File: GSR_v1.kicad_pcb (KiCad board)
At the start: 2 copper layers, 32.2 x 20.5 mm, 62 parts, among them P1 CONN_2, P2 CONN_2, P3 CONN_2, P4 CONN_2, Q1 DMP21D5UFB4-7B, U1 TPS63001, U2 LM324N, U3 NRF528XX-QFAA, U4 TMP116, U5 TPS2294x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

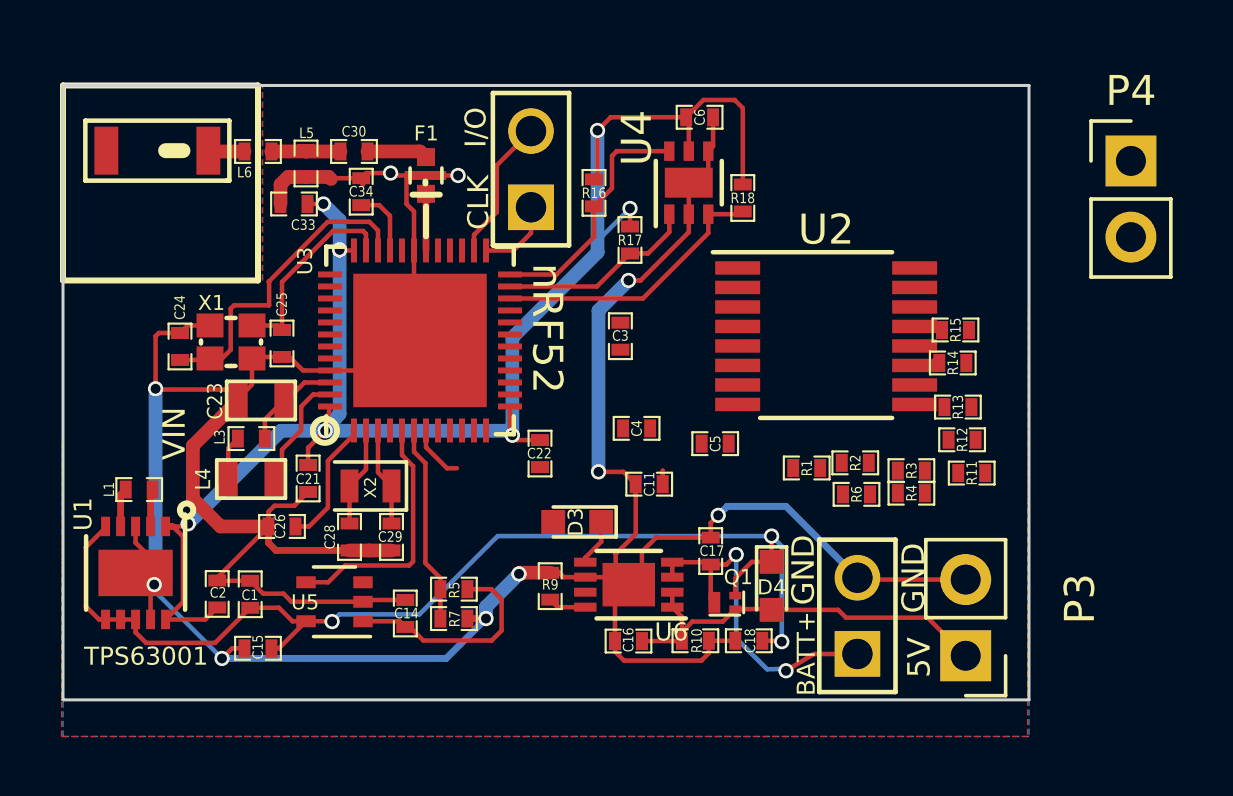
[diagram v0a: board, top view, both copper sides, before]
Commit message: Upgraded to KiCAD 5.0 compat
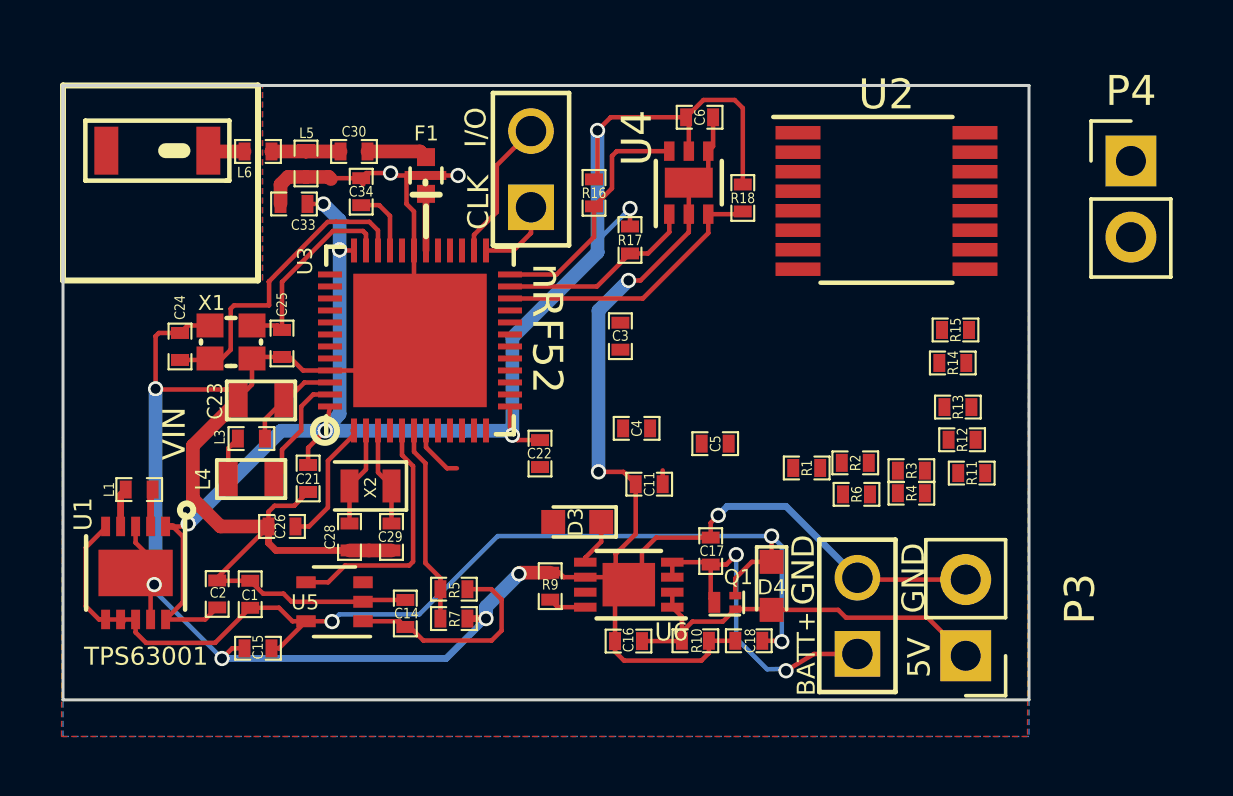
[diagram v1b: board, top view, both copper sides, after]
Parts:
- moved U2 4.94 mm to (293.4, 129.3)
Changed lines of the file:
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@@
 (kicad_pcb (version 4) (host pcbnew 4.0.6)
   (general
-    (links 162)
+    (links 0)
     (no_connects 33)
-    (area 265.849999 125.449999 298.150001 146.030001)
+    (area 264.8176 122.157123 320.907143 147.200001)
     (thickness 1.6)
     (drawings 26)
@@
   )
   (module Housings_SSOP:TSSOP-16_4.4x5mm_Pitch0.65mm (layer F.Cu)
-    (at 291.338 133.858)
+    (at 293.35 129.35)
     (descr "16-Lead Plastic Thin Shrink Small Outline (ST)-4.4 mm Body [TSSOP] (see Microchip Packaging Specification 00000049BS.pdf)")
     (tags "SSOP 0.65")

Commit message: Updated footprint for LM324
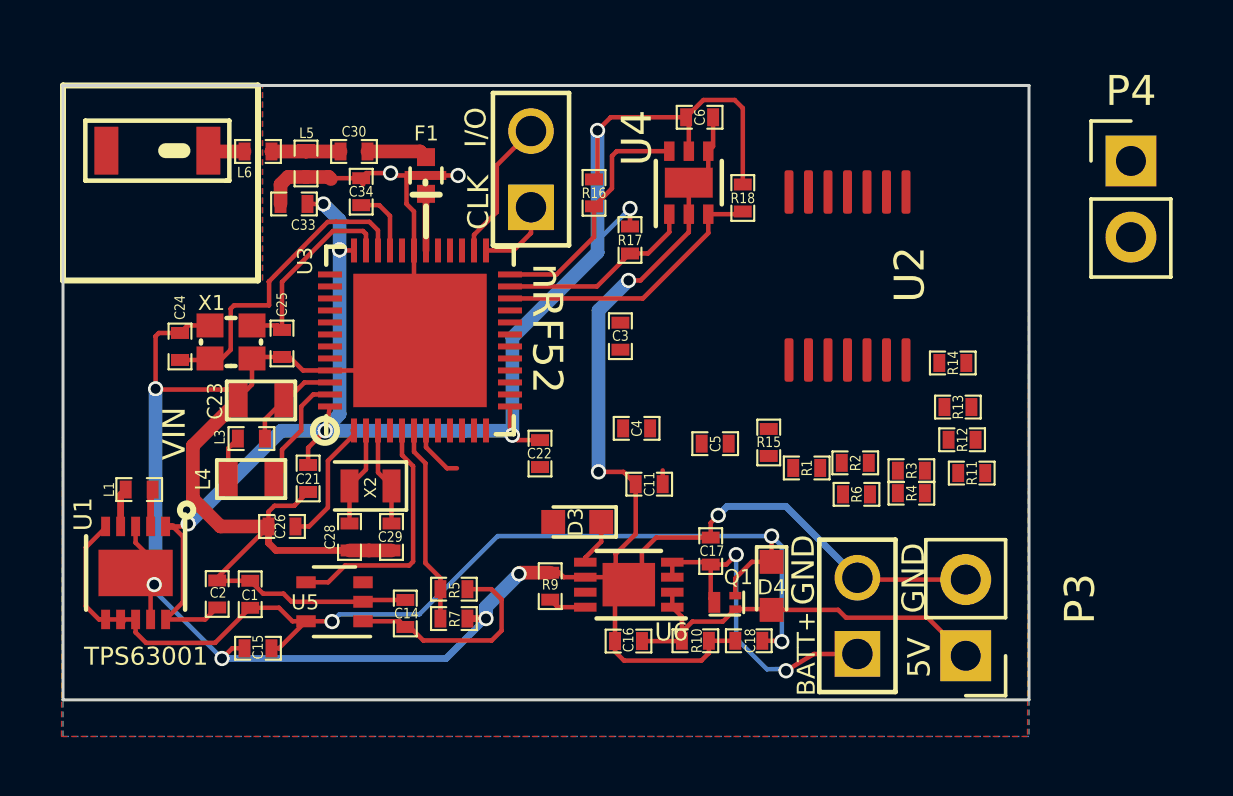
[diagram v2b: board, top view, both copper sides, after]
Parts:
- U2: footprint Housings_SSOP:TSSOP-16_4.4x5mm_Pitch0.65mm -> musaPwrPad:TSSOP-14_6.4x5mm
- moved R15 7.27 mm to (289.4, 137.4), turned to 270 degrees
- moved U2 2.82 mm to (292.1, 131.8), turned to 270 degrees

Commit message: Nathan edits and my finalization to PCB design.
Co-Authored-By: nzavanelli <nzavanelli@users.noreply.github.com>
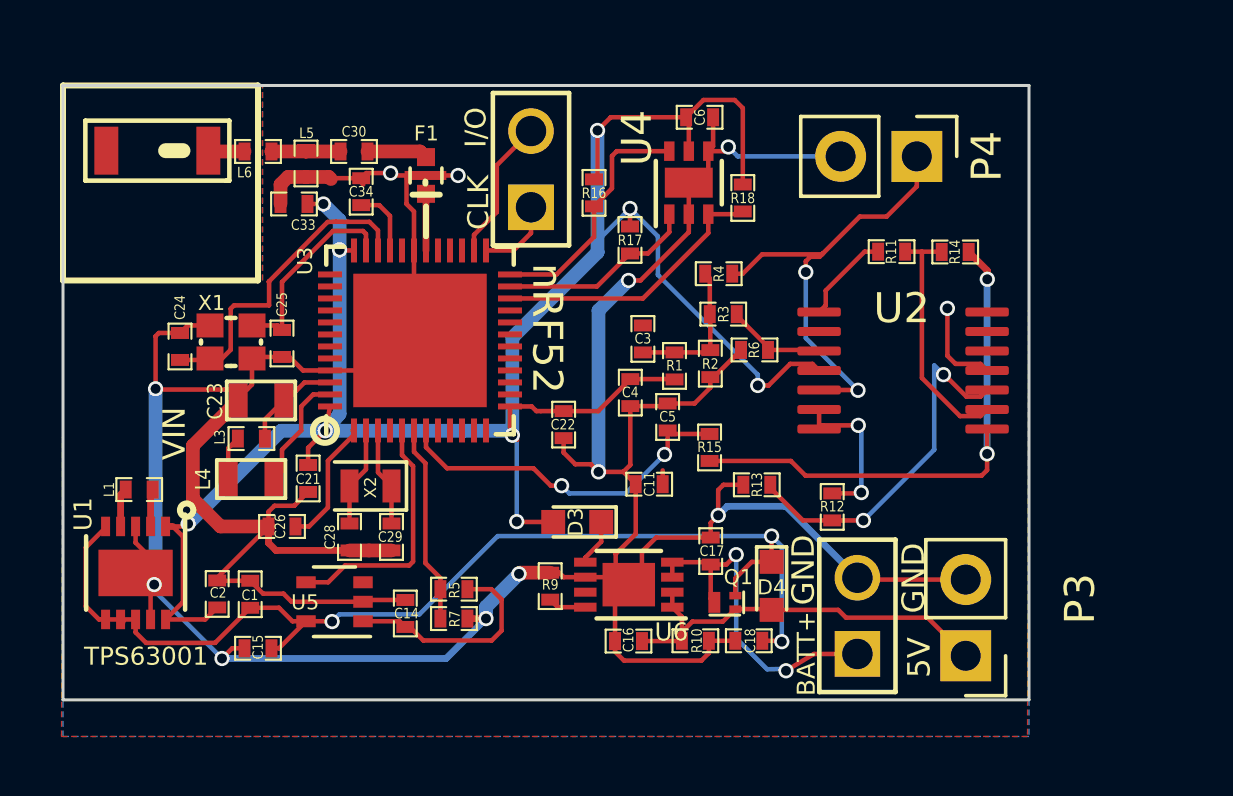
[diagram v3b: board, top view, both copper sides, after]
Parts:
- moved R4 9.73 mm to (287.8, 131.8)
- moved R3 8.16 mm to (287.9, 133.1)
- moved R11 7.85 mm to (293.5, 131.0), turned to 0 degrees
- moved R13 7.19 mm to (289.0, 138.8)
- moved P4 7.14 mm to (294.4, 127.9), turned to 270 degrees
- moved R6 5.89 mm to (289.0, 134.3), turned to 0 degrees
- moved R2 5.86 mm to (287.5, 134.8), turned to 90 degrees
- moved R1 5.57 mm to (286.3, 134.8), turned to 270 degrees
- moved R12 4.87 mm to (291.5, 139.5), turned to 270 degrees
- moved R14 3.70 mm to (295.6, 131.1), turned to 0 degrees
- moved U2 3.66 mm to (293.9, 135.0), turned to 0 degrees
- moved R15 1.98 mm to (287.5, 137.6)
- moved C5 1.82 mm to (286.1, 136.6), turned to 270 degrees
- moved C22 1.25 mm to (282.6, 136.8)
- moved C4 1.21 mm to (284.8, 135.7), turned to 270 degrees
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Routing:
- net DVDD: track 56.5 -> 76.1 mm, vias 7 -> 9
- net DGND: track 136.9 -> 155.2 mm, vias 10 -> 12
- net Net-(R14-Pad2): track 0.00 -> 17.9 mm, vias 0 -> 2
- net /ELECTRODE_INPUT: track 0.00 -> 15.4 mm, vias 0 -> 2
- net Net-(R12-Pad2): track 0.00 -> 12.1 mm, vias 0 -> 2
- net /GSR_AIN: track 1.88 -> 12.0 mm, vias 0 -> 2
- net Net-(R11-Pad2): track 0.00 -> 8.23 mm
- net Net-(R12-Pad1): track 0.00 -> 5.27 mm, vias 0 -> 2
- net Net-(C3-Pad2): track 0.00 -> 4.90 mm
- net Net-(R3-Pad1): track 0.00 -> 3.34 mm
- net Net-(R11-Pad1): track 0.00 -> 3.09 mm

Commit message: Fixed missing connections, resolved issues.
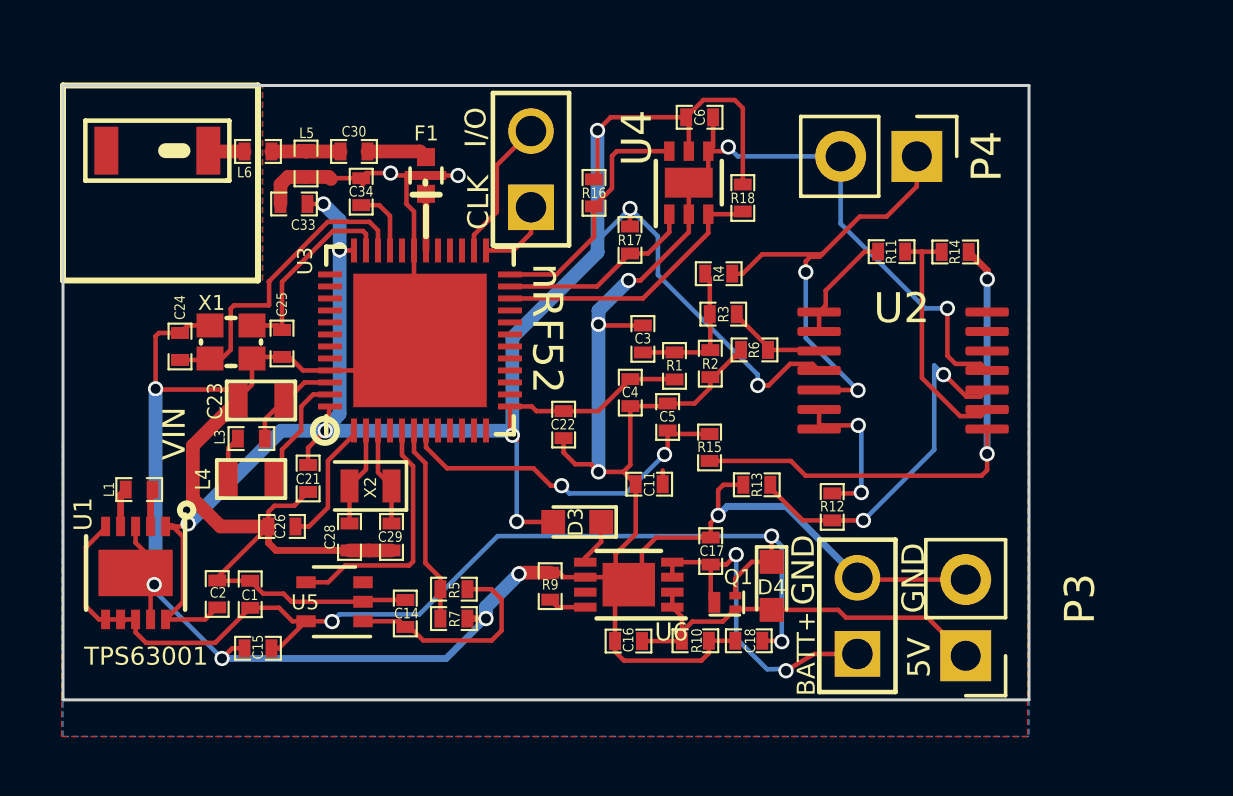
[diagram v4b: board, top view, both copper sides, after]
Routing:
- net DGND: track 155.2 -> 163.7 mm, vias 12 -> 13
- net Net-(R11-Pad1): track 3.09 -> 3.74 mm
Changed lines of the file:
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@@
     (thickness 1.6)
     (drawings 26)
-    (tracks 532)
+    (tracks 540)
     (zones 0)
     (modules 62)
@@
   (segment (start 286.76 129.79) (end 286.76 130.39) (width 0.152) (layer F.Cu) (net 37))
   (via (at 283.75 138.38) (size 0.508) (drill 0.3302) (layers F.Cu B.Cu) (net 37))
-  (segment (start 283.75 133) (end 283.75 138.38) (width 0.4572) (layer B.Cu) (net 37))
   (segment (start 284.75 132) (end 283.75 133) (width 0.4572) (layer B.Cu) (net 37))
   (via (at 284.75 132) (size 0.508) (drill 0.3302) (layers F.Cu B.Cu) (net 37))
@@
   (segment (start 295.65029 134.78029) (end 295.38 134.51) (width 0.152) (layer F.Cu) (net 37))
   (segment (start 295.38 134.51) (end 295.38 132.93) (width 0.152) (layer F.Cu) (net 37))
+  (via (at 283.75 133.46) (size 0.508) (drill 0.3302) (layers F.Cu B.Cu) (net 37))
+  (segment (start 283.75 133.46) (end 283.75 138.38) (width 0.4572) (layer B.Cu) (net 37))
+  (segment (start 283.75 133) (end 283.75 133.46) (width 0.4572) (layer B.Cu) (net 37))
+  (segment (start 283.78916 133.49916) (end 283.75 133.46) (width 0.152) (layer F.Cu) (net 37))
+  (segment (start 285.23 133.49916) (end 283.78916 133.49916) (width 0.152) (layer F.Cu) (net 37))
+  (segment (start 295.38 132.93) (end 294.65 132.93) (width 0.152) (layer B.Cu) (net 37))
+  (segment (start 291.8206 130.1006) (end 291.8206 127.8636) (width 0.152) (layer B.Cu) (net 37))
+  (segment (start 294.65 132.93) (end 291.8206 130.1006) (width 0.152) (layer B.Cu) (net 37))
   (segment (start 287.4772 133.13918) (end 287.45942 133.1214) (width 0.152) (layer F.Cu) (net 38))
   (segment (start 287.4772 134.32282) (end 287.4772 133.13918) (width 0.152) (layer F.Cu) (net 38))
@@
   (segment (start 292.62 131.04) (end 293.07084 131.04) (width 0.152) (layer F.Cu) (net 55))
   (segment (start 291.32411 132.33589) (end 292.62 131.04) (width 0.152) (layer F.Cu) (net 55))
+  (segment (start 291.1034 133.701) (end 291.1034 133.051) (width 0.152) (layer F.Cu) (net 55))
   (segment (start 295.18042 131.04) (end 295.19042 131.05) (width 0.152) (layer F.Cu) (net 56))
   (segment (start 296.48269 136.52171) (end 295.80171 136.52171) (width 0.152) (layer F.Cu) (net 56))

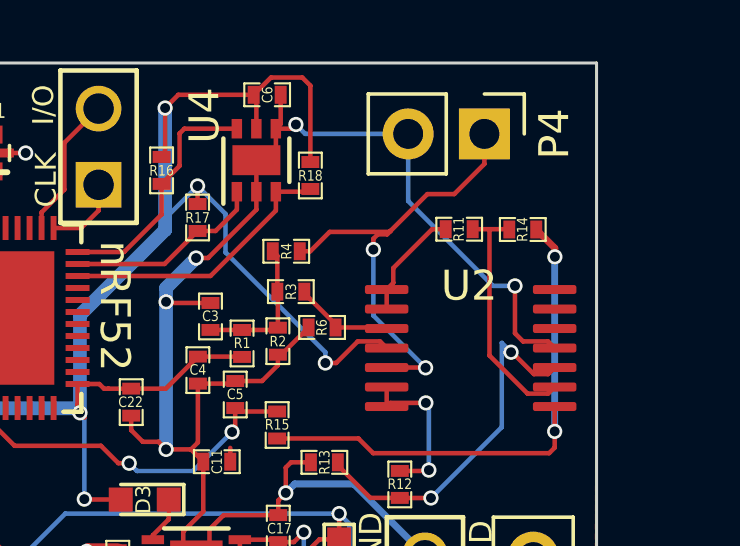
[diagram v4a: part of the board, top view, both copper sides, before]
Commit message: Updated Gerbers, deleted old gerber files, minor details. Updated silkscreen (back)
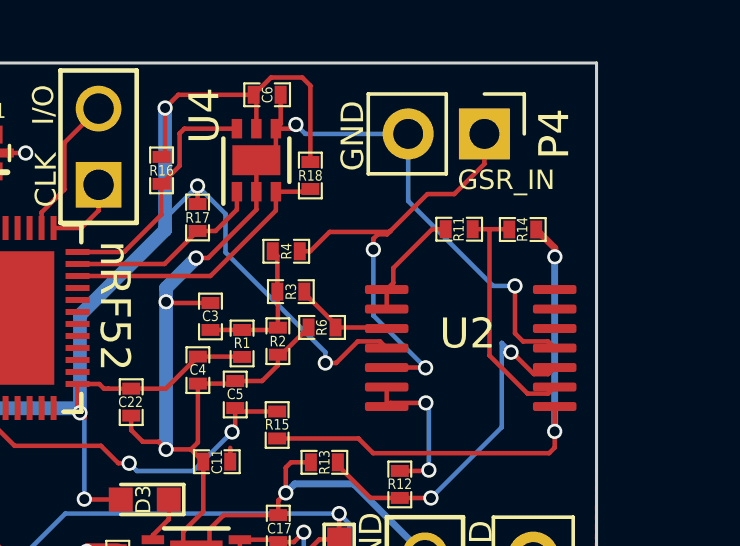
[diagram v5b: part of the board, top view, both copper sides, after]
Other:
- board text added: "GSR_IN"
- board text added: "nRF52-GSR Prototype 09/03/18 Yeo GaTech BNE Lab"
- board text removed: "nRF52-ADS1292-MPU ExG Prototype - 06/08/18 Yeo GaTech BNE Lab"
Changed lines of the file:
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@@
   (general
     (thickness 1.6)
-    (drawings 26)
+    (drawings 28)
     (tracks 540)
     (zones 0)
@@
     (34 B.Paste user)
     (35 F.Paste user hide)
-    (36 B.SilkS user hide)
+    (36 B.SilkS user)
     (37 F.SilkS user)
     (38 B.Mask user hide)
@@
   )
   (setup
-    (last_trace_width 0.152)
+    (last_trace_width 0.4572)
     (user_trace_width 0.152)
     (user_trace_width 0.229)
@@
     (visible_elements 7FFEFFBF)
     (pcbplotparams
-      (layerselection 0x010f0_80000001)
+      (layerselection 0x010f0_ffffffff)
       (usegerberextensions true)
       (usegerberattributes false)
@@
   (module musaPwrPad:TSSOP-14_6.4x5mm (layer F.Cu)
     (at 293.9034 135.001)
-    (fp_text reference U2 (at -0.05 -2.075 180) (layer F.SilkS)
+    (fp_text reference U2 (at -0.1034 -0.481 180) (layer F.SilkS)
       (effects (font (size 1 1) (thickness 0.15)))
     )
@@
       (net 9 DVDD))
   )
+  (gr_text GSR_IN (at 295.09 129.4) (layer F.SilkS)
+    (effects (font (size 0.65 0.65) (thickness 0.08)))
+  )
+  (gr_text GND (at 289.97 127.93 90) (layer F.SilkS)
+    (effects (font (size 0.75 0.75) (thickness 0.1)))
+  )
   (gr_text BATT+ (at 290.68 144.44 90) (layer F.SilkS)
     (effects (font (size 0.6 0.6) (thickness 0.07)))
@@
   )
   (gr_line (start 269.9 127.673) (end 269.32 127.673) (angle 90) (layer F.SilkS) (width 0.5))
-  (gr_text "nRF52-ADS1292-MPU\nExG Prototype - 06/08/18\nYeo GaTech BNE Lab" (at 273.975 142.56) (layer B.SilkS)
+  (gr_text "nRF52-GSR Prototype \n09/03/18\nYeo GaTech BNE Lab" (at 273.36 141.38) (layer B.SilkS)
     (effects (font (size 0.762 0.762) (thickness 0.127)) (justify mirror))
   )
